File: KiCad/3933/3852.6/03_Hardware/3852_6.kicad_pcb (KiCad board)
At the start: 2 copper layers, 52 x 30 mm, 53 parts, among them CN3 STRIP Prog., P1 SERIAL CONNECTOR, P2 JBAT, P3 TAMPER CONNECTOR, Q1 Q_NMOS_DGS, U1 SI4432B, U2 MSP430G2433IRHN32, U5 UPG2214TB

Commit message: Kicad and firmware updates
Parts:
- U1: footprint Housings_DFN_QFN:QFN-20-1EP_4x4mm_Pitch0.5mm -> saet:QFN-20-1EP_4x4mm_Pitch0.5mm_with_back_holes
- U2: footprint Housings_DFN_QFN:QFN-32-1EP_5x5mm_Pitch0.5mm -> saet:QFN-32-1EP_5x5mm_Pitch0.5mm_with_back_holes
- moved R2 2.27 mm to (140.5, 77.7), turned to 0 degrees
- moved C17 1.67 mm to (143.9, 87.4)
- moved Q1 1.02 mm to (139.4, 80.0), turned to 180 degrees
- moved QZ1 0.05 mm to (147.0, 95.5)
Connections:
- Q1 pad 1: /Yellow -> Net-(Q1-Pad1)
- Q1 pad 2: Net-(Q1-Pad2) -> /TX
- Q1 pad 3: /TX -> /Yellow
- QZ1 pad 2: Net-(QZ1-Pad2) -> (no net)
- QZ1 pad 3: (no net) -> Net-(QZ1-Pad2)
- R2 pad 1: Net-(Q1-Pad2) -> Net-(Q1-Pad1)
- U1 pad 21: (no net) -> GND
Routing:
- net GND: track 167.7 -> 305.4 mm, vias 9 -> 78
- net Net-(QZ1-Pad2): track 3.27 -> 6.97 mm
- net /TX: track 0.98 -> 3.18 mm
- net Net-(CN3-Pad7): track 18.7 -> 20.3 mm
- net VCC: track 85.8 -> 87.3 mm, vias 5 -> 4
- net Net-(Q1-Pad2): track 1.36 -> 0.00 mm
- net Net-(Q1-Pad1): track 0.00 -> 1.32 mm
- net CS: track 21.1 -> 22.3 mm
- net (no net): vias 62 -> 0

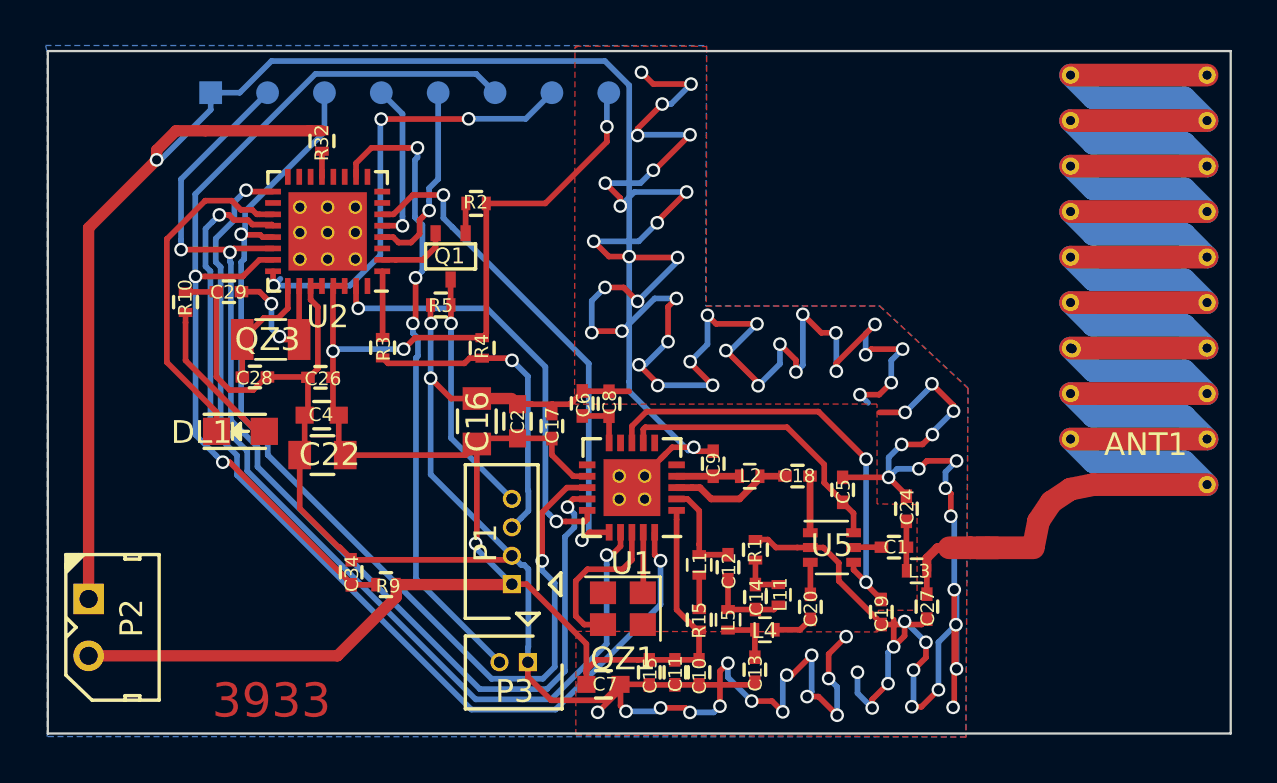
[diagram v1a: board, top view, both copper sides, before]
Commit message: Aggiornamenti su modulo SPI (sw->hw) e vari sui circuiti
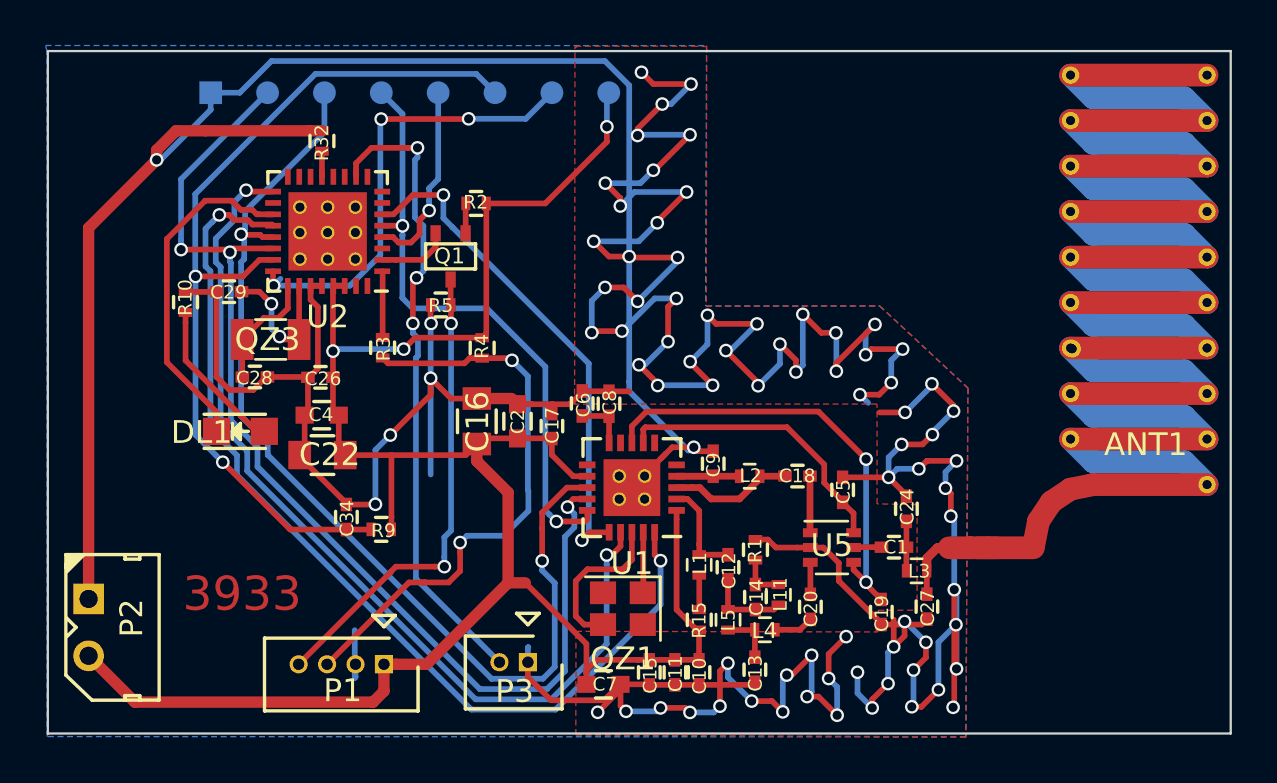
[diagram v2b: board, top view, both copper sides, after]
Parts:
- moved P1 6.64 mm to (136.5, 97.9), turned to 180 degrees
- moved R9 2.44 mm to (136.4, 92.0)
- moved C34 2.44 mm to (134.8, 91.4)
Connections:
- CN3 pad 4: Net-(CN3-Pad4) -> CLK
- U2 pad 31: CLK -> Net-(U2-Pad31)
- U2 pad 5: Net-(CN3-Pad4) -> CLK
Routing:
- net /White: track 13.9 -> 25.4 mm, vias 1 -> 2
- net /Yellow: track 10.8 -> 21.0 mm, vias 1 -> 2
- net GND: track 305.4 -> 296.8 mm, vias 78 -> 80
- net CLK: track 19.1 -> 26.6 mm
- net Net-(CN3-Pad4): track 7.13 -> 0.00 mm, vias 1 -> 0
- net VCC: track 87.3 -> 92.5 mm, vias 4 -> 3
- net Net-(C34-Pad1): track 40.7 -> 39.4 mm

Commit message: Inserimento buchi sul CS per alloggiare supporti in gomma
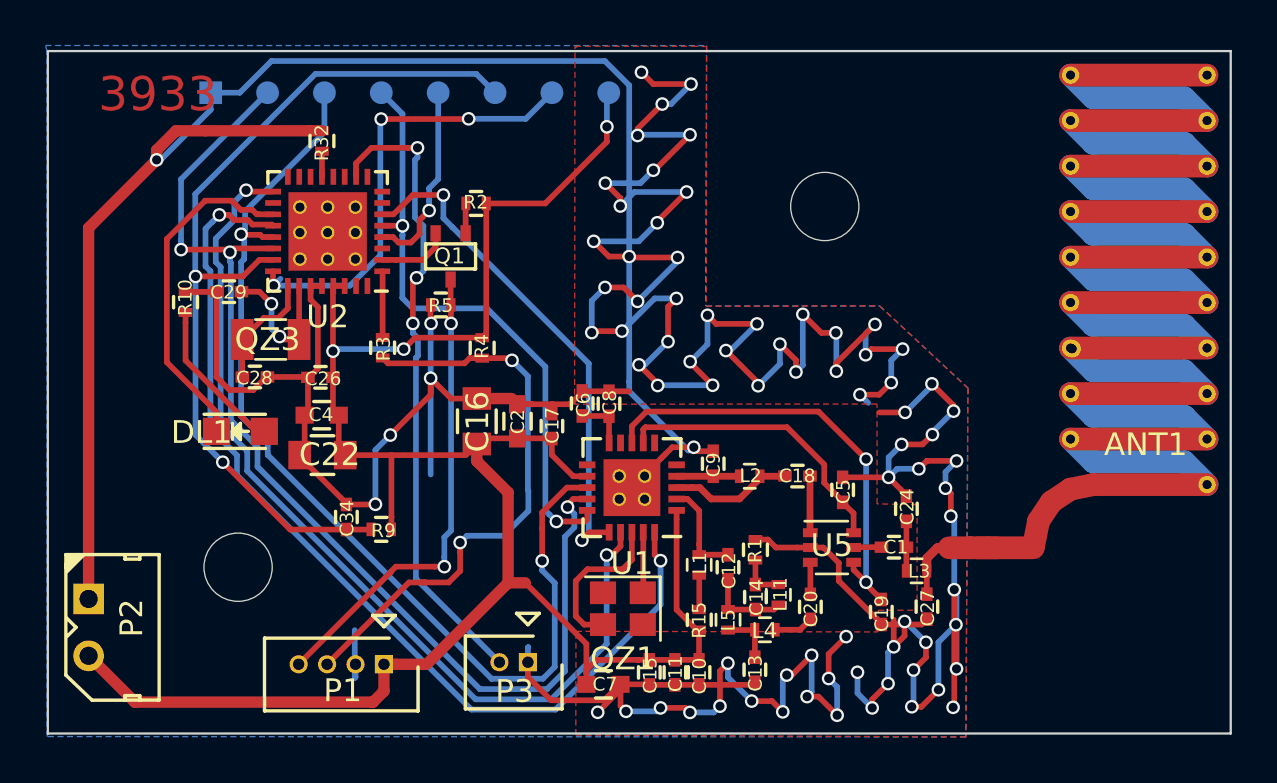
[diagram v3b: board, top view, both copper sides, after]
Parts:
- added HOLE_3mm: VAL**, saet:HOLE_3mm, F.Cu at (130.1, 93.6)
- added HOLE_3mm: VAL**, saet:HOLE_3mm, F.Cu at (155.9, 77.8)
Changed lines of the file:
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@@
     (links 114)
     (no_connects 0)
-    (area 105.855798 55.473481 173.747121 102.13946)
+    (area 121.647119 70.907439 173.747121 101.007441)
     (thickness 1.6)
     (drawings 7)
     (tracks 767)
     (zones 0)
-    (modules 53)
+    (modules 55)
     (nets 57)
   )
@@
     )
   )
-  (gr_text 3933 (at 130.24104 94.82328) (layer F.Cu)
+  (module saet:HOLE_3mm (layer F.Cu)
+    (at 130.0607 93.64726)
+    (fp_text reference HOLE_3mm (at 0 -2.5) (layer F.SilkS) hide
+      (effects (font (size 1 1) (thickness 0.15)))
+    )
+    (fp_text value VAL** (at 0 2.9) (layer F.Fab) hide
+      (effects (font (size 1 1) (thickness 0.15)))
+    )
+    (pad "" np_thru_hole circle (at 0 0) (size 3 3) (drill 3) (layers *.Cu *.Mask F.SilkS))
+  )
+  (module saet:HOLE_3mm (layer F.Cu)
+    (at 155.85186 77.79004)
+    (fp_text reference HOLE_3mm (at 0 -2.5) (layer F.SilkS) hide
+      (effects (font (size 1 1) (thickness 0.15)))
+    )
+    (fp_text value VAL** (at 0 2.9) (layer F.Fab) hide
+      (effects (font (size 1 1) (thickness 0.15)))
+    )
+    (pad "" np_thru_hole circle (at 0 0) (size 3 3) (drill 3) (layers *.Cu *.Mask F.SilkS))
+  )
+  (gr_text 3933 (at 126.5301 72.8599) (layer F.Cu)
     (effects (font (size 1.5 1.5) (thickness 0.3)))
   )
